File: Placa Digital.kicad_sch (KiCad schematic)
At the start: 9 parts, among them J1 SALIDAS, J2 HMI, J4 ENTRADAS, U1 ESP32-DEVKITC-32D, U2 Alimentación

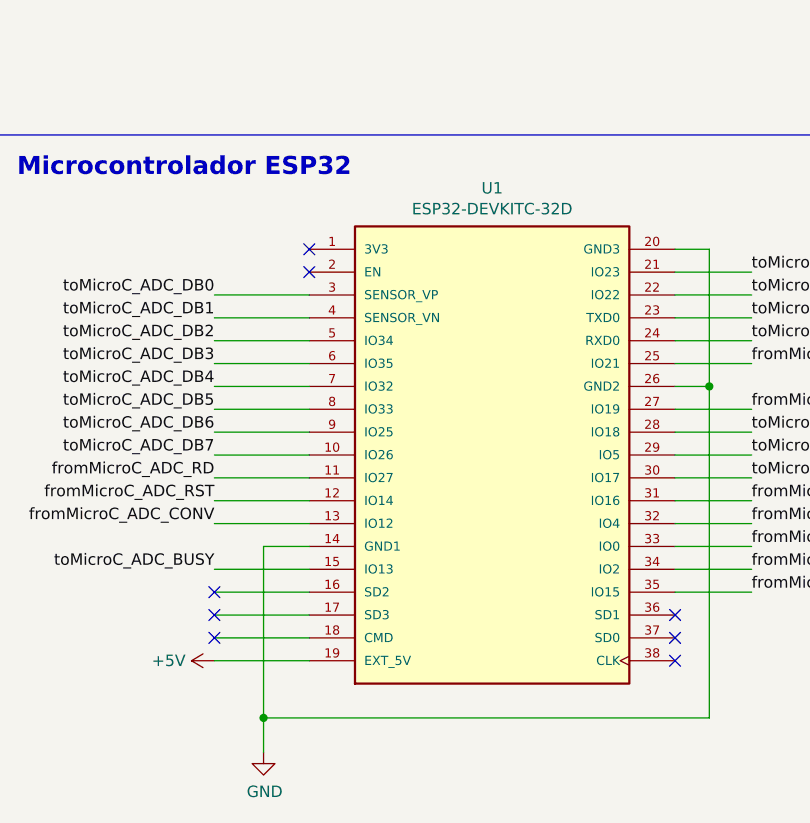
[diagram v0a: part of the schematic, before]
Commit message: Add 3d model + 1 Layer
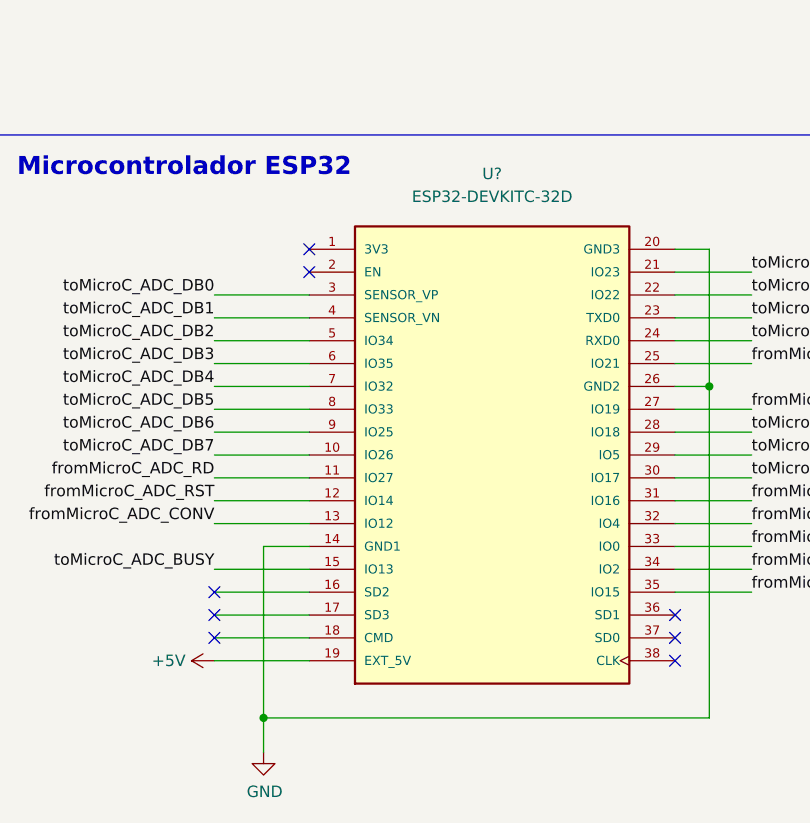
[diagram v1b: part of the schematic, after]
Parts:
- removed U1: ESP32-DEVKITC-32D, LIB_ESP32-DevKitC:DIP2600W100P254L5400H500Q38N, symbol ESP32-DEVKITC-32D:ESP32-DEVKITC-32D
- added U?: ESP32-DEVKITC-32D, MODULE_ESP32-DEVKITC-32D, symbol CEDCp:ESP32-DEVKITC-32D
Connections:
- net +5V: now also U?.19 (EXT_5V)
- net GND: now also U?.14 (GND1), U?.20 (GND3), U?.26 (GND2)
- net fromMicroC_A6841CLK1: now also U?.33 (IO0)
- net fromMicroC_A6841ST1: now also U?.35 (IO15)
- net fromMicroC_A6841SerialDataIN: now also U?.34 (IO2)
- net fromMicroC_ADC_CONV: now also U?.13 (IO12)
- net fromMicroC_ADC_RD: now also U?.11 (IO27)
- net fromMicroC_ADC_RST: now also U?.12 (IO14)
- net fromMicroC_DACI2C_SCL: now also U?.25 (IO21)
- net fromMicroC_DACI2C_SDA: now also U?.27 (IO19)
- net fromMicroC_DisplaySCLK: now also U?.31 (IO16)
- net fromMicroC_DisplaySID: now also U?.32 (IO4)
- net toMicroC_ADC_BUSY: now also U?.15 (IO13)
- net toMicroC_ADC_DB0: now also U?.3 (SENSOR_VP)
- net toMicroC_ADC_DB1: now also U?.4 (SENSOR_VN)
- net toMicroC_ADC_DB2: now also U?.5 (IO34)
- net toMicroC_ADC_DB3: now also U?.6 (IO35)
- net toMicroC_ADC_DB4: now also U?.7 (IO32)
- net toMicroC_ADC_DB5: now also U?.8 (IO33)
- net toMicroC_ADC_DB6: now also U?.9 (IO25)
- net toMicroC_ADC_DB7: now also U?.10 (IO26)
- net toMicroC_Button1: now also U?.21 (IO23)
- net toMicroC_Button2: now also U?.22 (IO22)
- net toMicroC_Button3: now also U?.23 (TXD0)
- net toMicroC_EncoderButton: now also U?.30 (IO17)
- net toMicroC_EncoderSignalA: now also U?.28 (IO18)
- net toMicroC_EncoderSignalB: now also U?.29 (IO5)
- net toMicroC_OverVoltageSignal: now also U?.24 (RXD0)

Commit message: Version V1 (Clearence)
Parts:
- gave numbers to parts that had none: 1
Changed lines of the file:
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@@
   (symbol (lib_id "CEDCp:ESP32-DEVKITC-32D") (at 149.733 94.742 0) (unit 1)
     (in_bom yes) (on_board yes) (fields_autoplaced)
-    (property "Reference" "U?" (id 0) (at 149.733 63.5 0))
+    (property "Reference" "U1" (id 0) (at 149.733 63.5 0))
     (property "Value" "ESP32-DEVKITC-32D" (id 1) (at 149.733 66.04 0))
     (property "Footprint" "MODULE_ESP32-DEVKITC-32D" (id 2) (at 149.733 94.742 0)
@@
       (reference "J4") (unit 1) (value "ENTRADAS") (footprint "Connector_PinHeader_2.54mm:PinHeader_1x10_P2.54mm_Vertical")
     )
+    (path "/2e3b42a4-4d62-4710-9908-15b94331306e"
+      (reference "U1") (unit 1) (value "ESP32-DEVKITC-32D") (footprint "MODULE_ESP32-DEVKITC-32D")
+    )
     (path "/7ab1537a-270e-4f16-a302-0f725f4cb04d"
       (reference "U2") (unit 1) (value "Alimentación") (footprint "CEDCp:Bornera_1x2")
     )
-    (path "/2e3b42a4-4d62-4710-9908-15b94331306e"
-      (reference "U?") (unit 1) (value "ESP32-DEVKITC-32D") (footprint "MODULE_ESP32-DEVKITC-32D")
-    )
   )
